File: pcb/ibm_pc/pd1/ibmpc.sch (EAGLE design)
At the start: 47 parts, among them IC1 STM32F072C8T6, SW1 324_SW, SW2 324_SW, U1 MAX3232

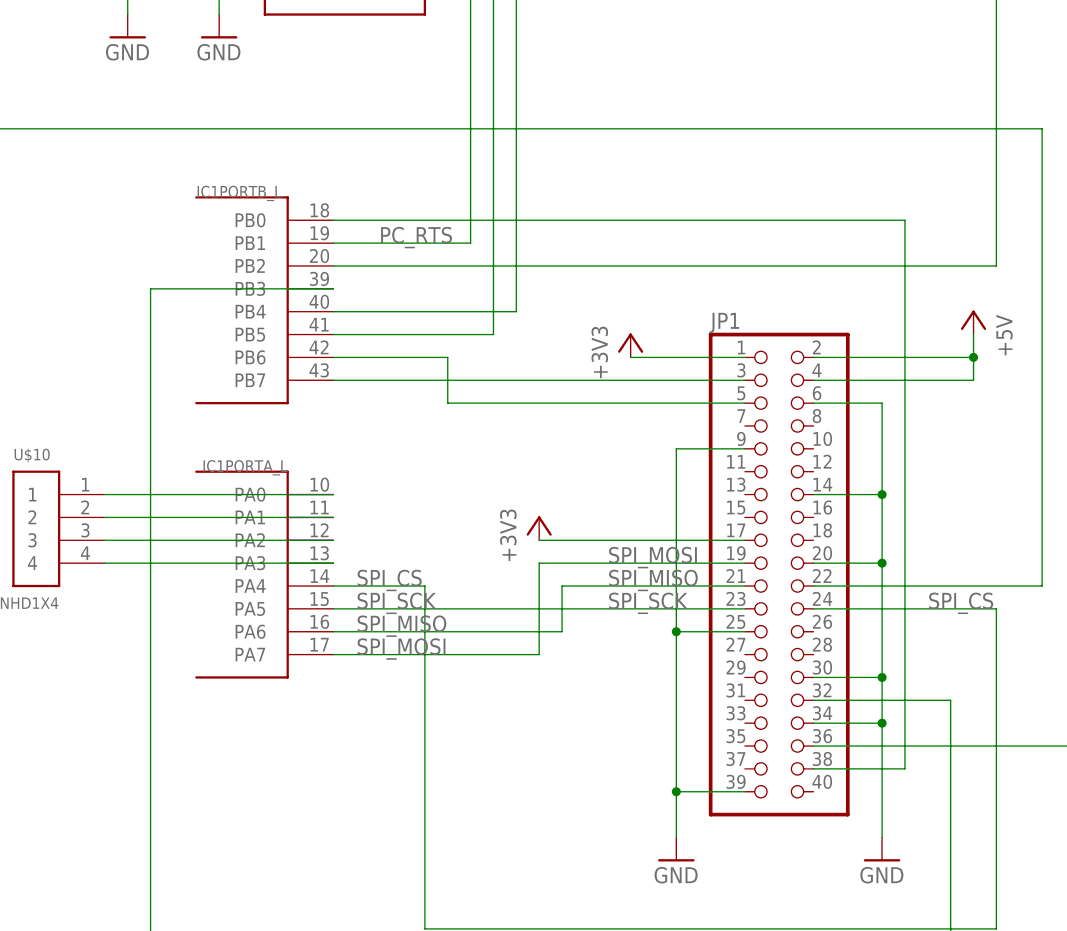
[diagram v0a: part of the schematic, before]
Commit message: added BUSY to ibm card
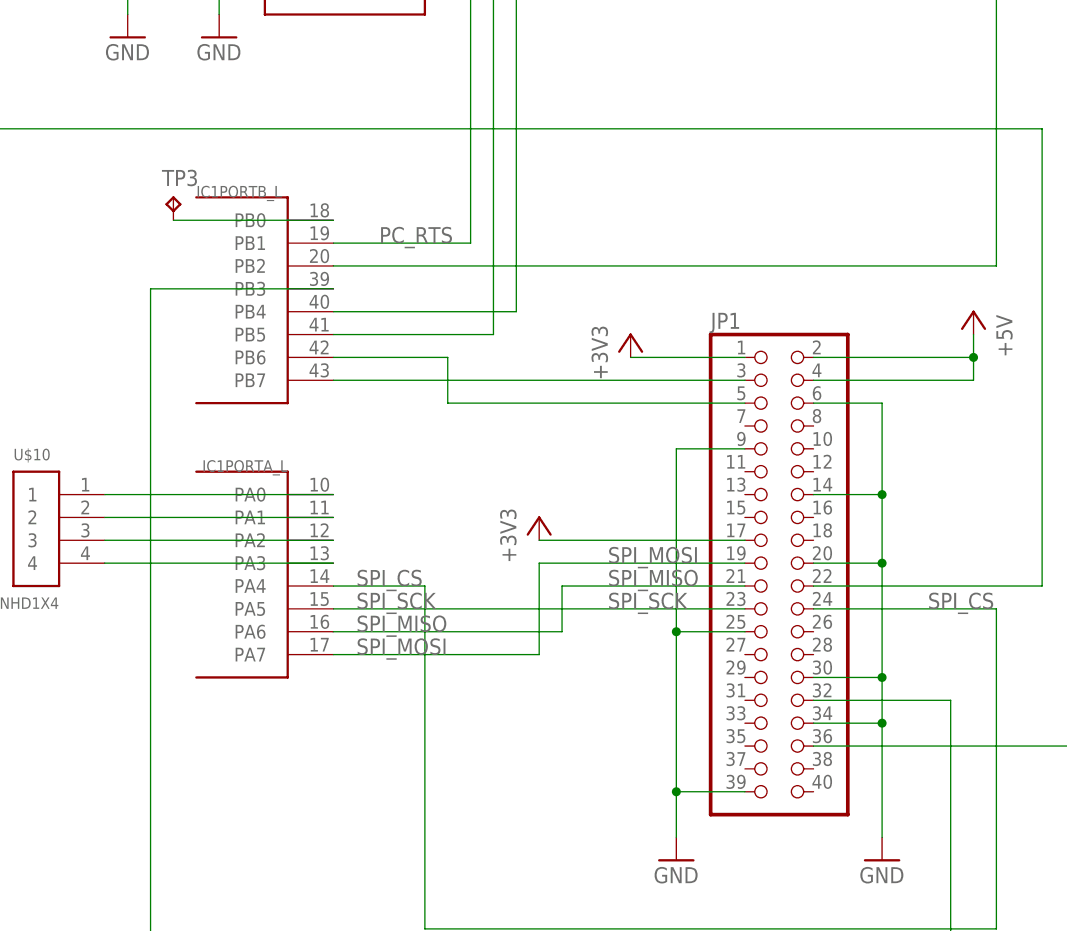
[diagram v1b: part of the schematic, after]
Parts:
- added TP3: TPTP12R, testpad:TPTP12R
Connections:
- removed net N$3: IC1PORTB_L.PB0, JP1.38
- new net N$45: IC1PORTB_L.PB0, TP3.TP
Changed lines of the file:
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@@
 <part name="GND25" library="backplane" deviceset="GND" device=""/>
 <part name="U$10" library="adafruit_changed" deviceset="PINHD1X4" device=""/>
+<part name="TP3" library="testpad" library_urn="urn:adsk.eagle:library:385" deviceset="TP" device="TP12R" package3d_urn="urn:adsk.eagle:package:27963/1"/>
 <part name="R1" library="SparkFun-Passives" deviceset="RESISTOR" device="0805-RES" value="5.1K"/>
 <part name="R2" library="SparkFun-Passives" deviceset="RESISTOR" device="0805-RES" value="5.1K"/>
@@
 <attribute name="VALUE" x="12.7" y="15.24" size="1.27" layer="96" font="vector" rot="MR0"/>
 </instance>
+<instance part="TP3" gate="G$1" x="25.4" y="60.96" smashed="yes">
+<attribute name="NAME" x="24.13" y="62.23" size="1.778" layer="95"/>
+<attribute name="TP_SIGNAL_NAME" x="26.67" y="59.69" size="1.778" layer="97"/>
+</instance>
 <instance part="R1" gate="G$1" x="129.54" y="170.18" smashed="yes" rot="R180">
 <attribute name="NAME" x="133.35" y="168.6814" size="1.778" layer="95" rot="R180"/>
@@
 </segment>
 </net>
+<net name="N$45" class="0">
+<segment>
+<pinref part="TP3" gate="G$1" pin="TP"/>
+<pinref part="IC1" gate="PORTB_L" pin="PB0"/>
+<wire x1="25.4" y1="58.42" x2="43.18" y2="58.42" width="0.1524" layer="91"/>
+</segment>
+</net>
 <net name="N$31" class="0">
 <segment>
@@
 </segment>
 </net>
-<net name="N$3" class="0">
-<segment>
-<pinref part="IC1" gate="PORTB_L" pin="PB0"/>
-<wire x1="43.18" y1="58.42" x2="106.68" y2="58.42" width="0.1524" layer="91"/>
-<wire x1="106.68" y1="58.42" x2="106.68" y2="-2.54" width="0.1524" layer="91"/>
-<pinref part="JP1" gate="A" pin="38"/>
-<wire x1="106.68" y1="-2.54" x2="96.52" y2="-2.54" width="0.1524" layer="91"/>
-</segment>
-</net>
